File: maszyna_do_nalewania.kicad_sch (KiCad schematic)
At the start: 30 parts, among them J1 USB_C_Receptacle_USB2.0_16P, J2 SMA_RP, U1 ESP32-C3, Y1 40Mhz 10ppm

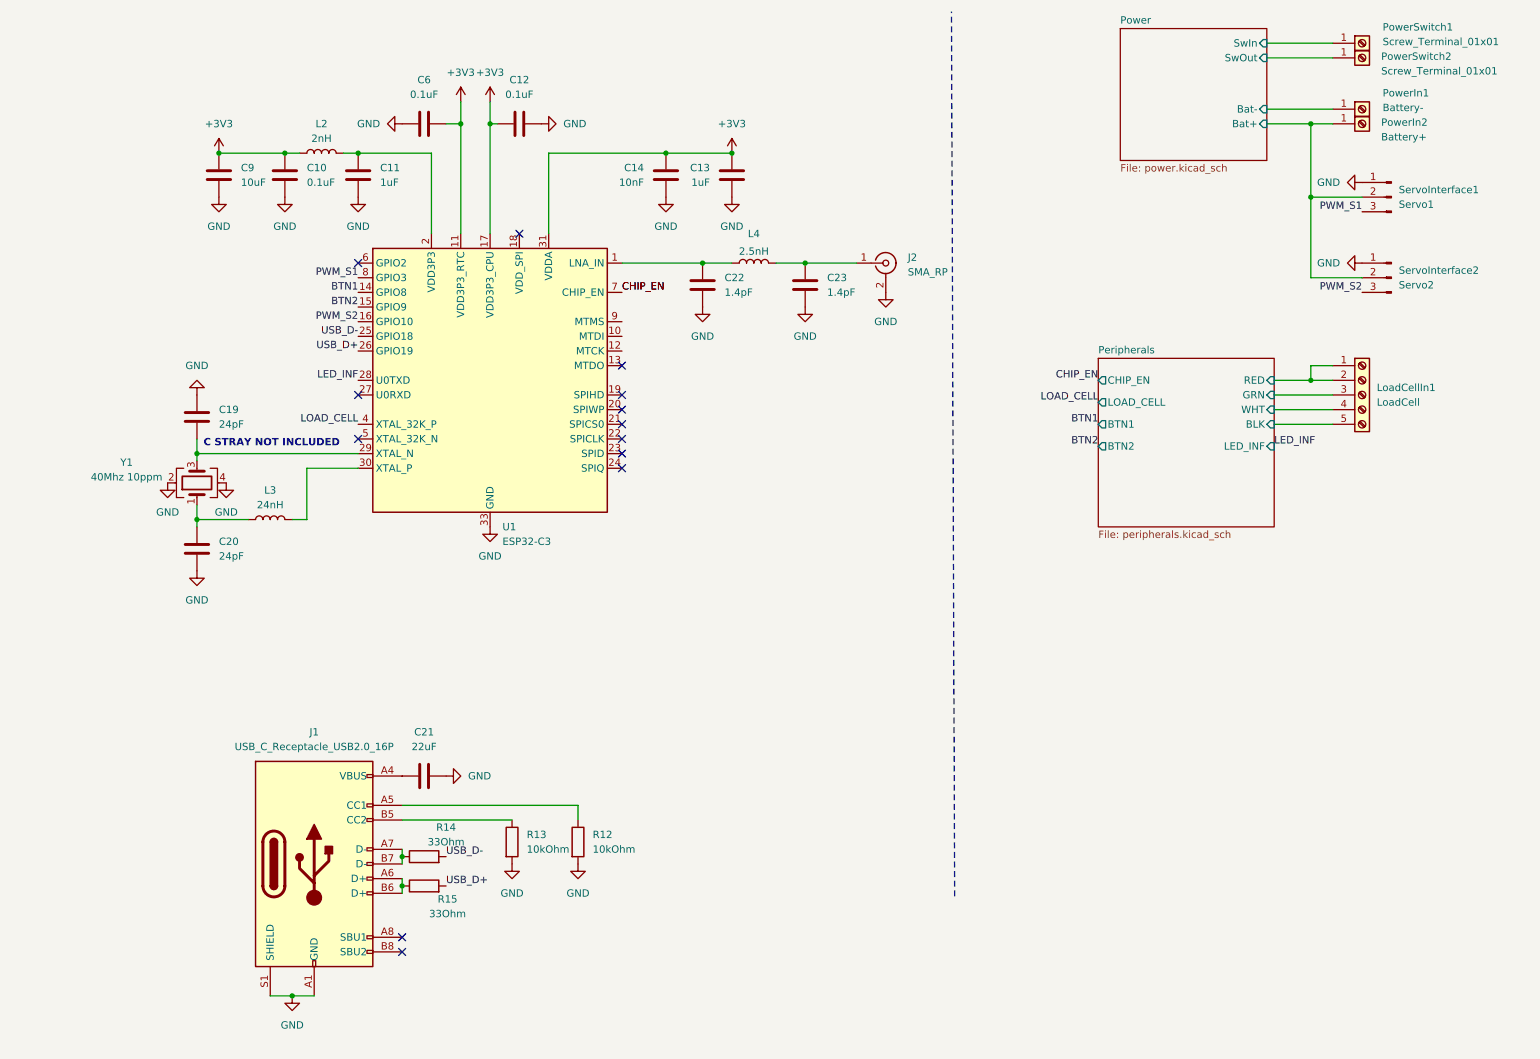
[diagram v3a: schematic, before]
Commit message: feat: pcb almost done, added rgb led
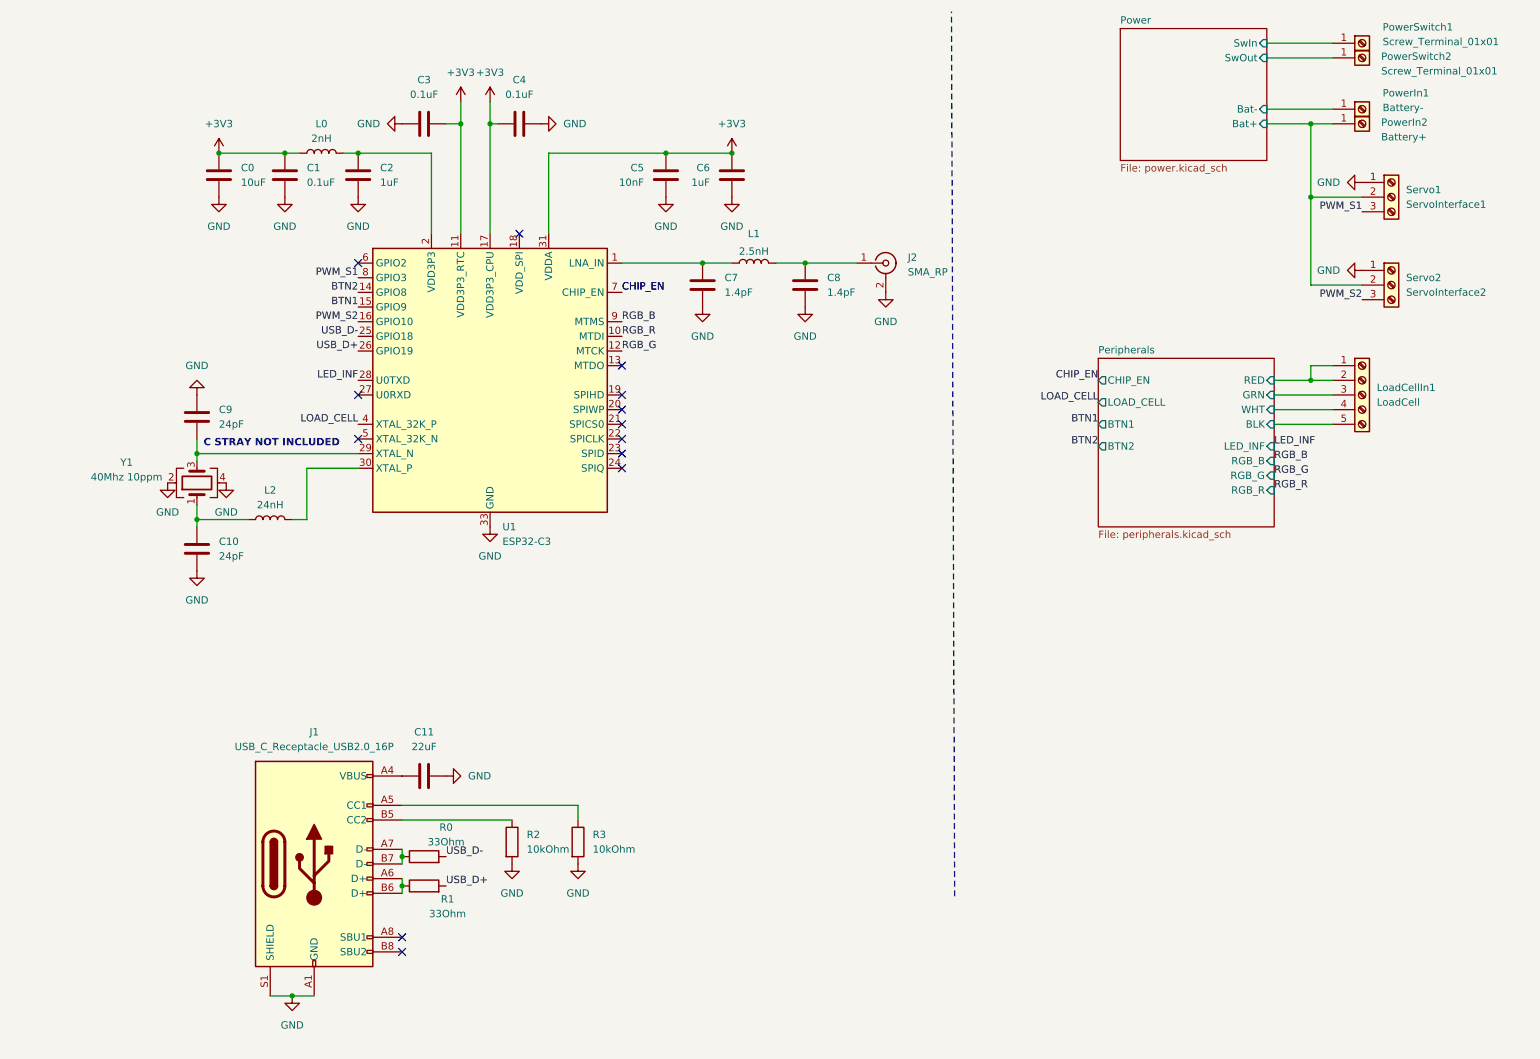
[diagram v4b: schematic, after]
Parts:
- removed ServoInterface1: Servo1, Connector_PinHeader_1.00mm:PinHeader_1x03_P1.00mm_Vertical, symbol Connector:Conn_01x03_Pin
- removed ServoInterface2: Servo2, Connector_PinHeader_1.00mm:PinHeader_1x03_P1.00mm_Vertical, symbol Connector:Conn_01x03_Pin
- added Servo1: ServoInterface1, TerminalBlock:TerminalBlock_MaiXu_MX126-5.0-03P_1x03_P5.00mm, symbol Connector:Screw_Terminal_01x03
- added Servo2: ServoInterface2, TerminalBlock:TerminalBlock_MaiXu_MX126-5.0-03P_1x03_P5.00mm, symbol Connector:Screw_Terminal_01x03
- C10: renamed from C20; footprint Capacitor_SMD:C_0805_2012Metric_Pad1.18x1.45mm_HandSolder -> Capacitor_SMD:C_0402_1005Metric
- C9: renamed from C19; footprint Capacitor_SMD:C_0805_2012Metric_Pad1.18x1.45mm_HandSolder -> Capacitor_SMD:C_0402_1005Metric
- R1: renamed from R15; footprint Resistor_SMD:R_0402_1005Metric_Pad0.72x0.64mm_HandSolder -> Resistor_SMD:R_0402_1005Metric
- renumbered C9 to C0, C10 to C1, C21 to C11, C11 to C2, C6 to C3, C12 to C4, C14 to C5, C13 to C6, C22 to C7, C23 to C8, L2 to L0, L4 to L1, L3 to L2, R14 to R0, R13 to R2, R12 to R3
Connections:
- net BTN1: now also U1.15 (GPIO9); no longer U1.14 (GPIO8)
- net BTN2: now also U1.14 (GPIO8); no longer U1.15 (GPIO9)
- net GND: now also Servo1.1 (Pin_1), Servo2.1 (Pin_1)
- net PWM_S1: now also Servo1.3 (Pin_3)
- net PWM_S2: now also Servo2.3 (Pin_3)
- net Power/Bat+: now also Servo1.2 (Pin_2), Servo2.2 (Pin_2)
- net RGB_R: now reaches U1.10 (MTDI)
- net RGB_G: now reaches U1.12 (MTCK)
- net RGB_B: now reaches U1.9 (MTMS)
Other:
- sheet Peripherals ports: added RGB_B, RGB_G, RGB_R; removed none

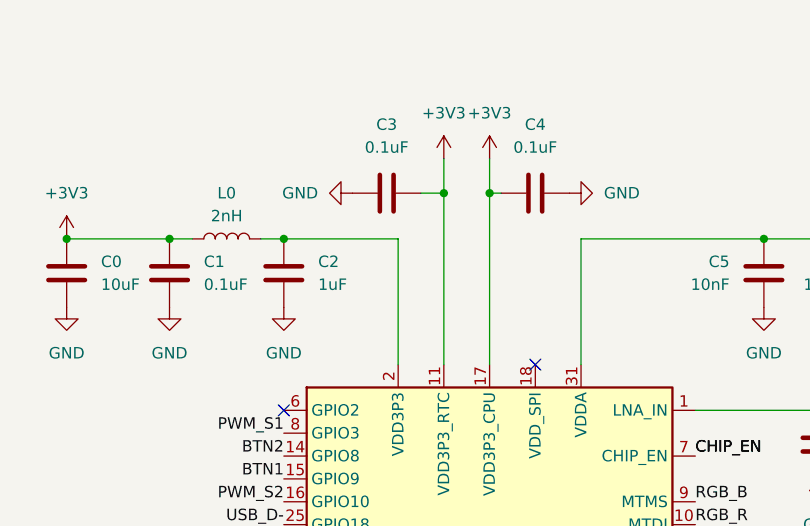
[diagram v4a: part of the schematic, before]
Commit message: feat: silkscreen done
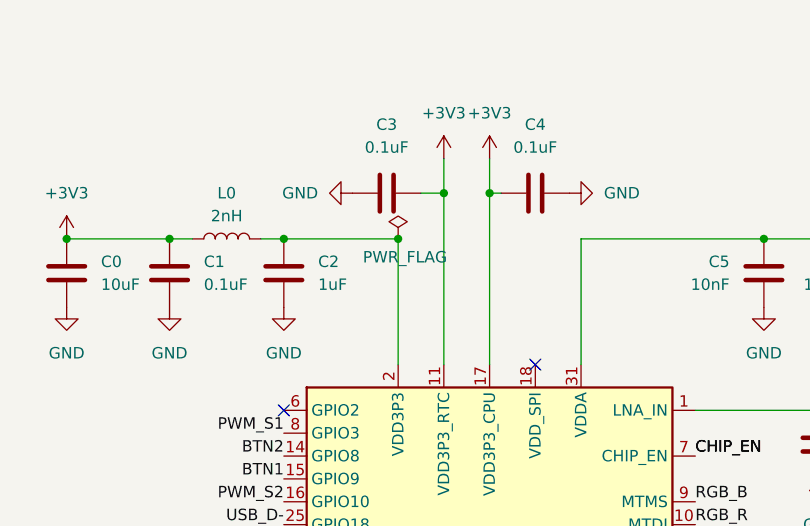
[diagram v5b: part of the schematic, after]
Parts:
- J1: footprint Connector_USB:USB_C_Receptacle_GCT_USB4085 -> Connector_USB:USB_C_Receptacle_HRO_TYPE-C-31-M-12
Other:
- company: (none) -> Mateusz Drogowski Karol Dworczyński
- title: (none) -> Drink Pouring Machine
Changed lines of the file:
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@@
 	(paper "A4")
 	(title_block
+		(title "Drink Pouring Machine")
 		(date "2025-12-08")
+		(rev "v1.0")
+		(company "Mateusz Drogowski Karol Dworczyński")
 	)
 	(text "C STRAY NOT INCLUDED"
@@
 		(color 0 0 0 0)
 	)
+	(junction
+		(at 86.36 36.83)
+		(diameter 0)
+		(color 0 0 0 0)
+	)
 	(no_connect
 		(at 73.66 86.36)
@@
 	)
 	(symbol
+		(lib_id "power:PWR_FLAG")
+		(at 86.36 36.83 0)
+		(unit 1)
+		(exclude_from_sim no)
+		(in_bom yes)
+		(on_board yes)
+		(dnp no)
+		(property "Reference" "#FLG04"
+			(at 86.36 34.925 0)
+			(effects
+				(font
+					(size 1.27 1.27)
+				)
+				(hide yes)
+			)
+		)
+		(property "Value" "PWR_FLAG"
+			(at 87.122 38.862 0)
+			(effects
+				(font
+					(size 1.27 1.27)
+				)
+			)
+		)
+		(property "Footprint" ""
+			(at 86.36 36.83 0)
+			(effects
+				(font
+					(size 1.27 1.27)
+				)
+				(hide yes)
+			)
+		)
+		(property "Datasheet" "~"
+			(at 86.36 36.83 0)
+			(effects
+				(font
+					(size 1.27 1.27)
+				)
+				(hide yes)
+			)
+		)
+		(property "Description" "Special symbol for telling ERC where power comes from"
+			(at 86.36 36.83 0)
+			(effects
+				(font
+					(size 1.27 1.27)
+				)
+				(hide yes)
+			)
+		)
+		(pin "1"
+		)
+		(instances
+			(project ""
+				(path "/9edf3a40-33ab-40a8-8c54-e53c70f0a44f"
+					(reference "#FLG04")
+					(unit 1)
+				)
+			)
+		)
+	)
+	(symbol
 		(lib_id "power:+3V3")
 		(at 138.43 36.83 0)
@@
 			)
 		)
-		(property "Footprint" "Connector_USB:USB_C_Receptacle_GCT_USB4085"
+		(property "Footprint" "Connector_USB:USB_C_Receptacle_HRO_TYPE-C-31-M-12"
 			(at 69.85 160.02 0)
 			(effects

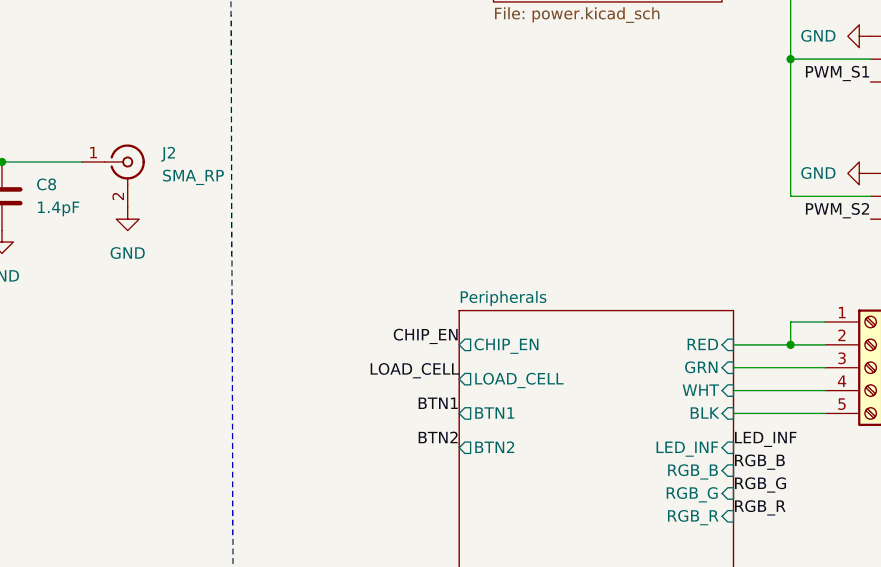
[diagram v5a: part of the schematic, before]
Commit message: fix: led resistor values, tensometer screw terminal
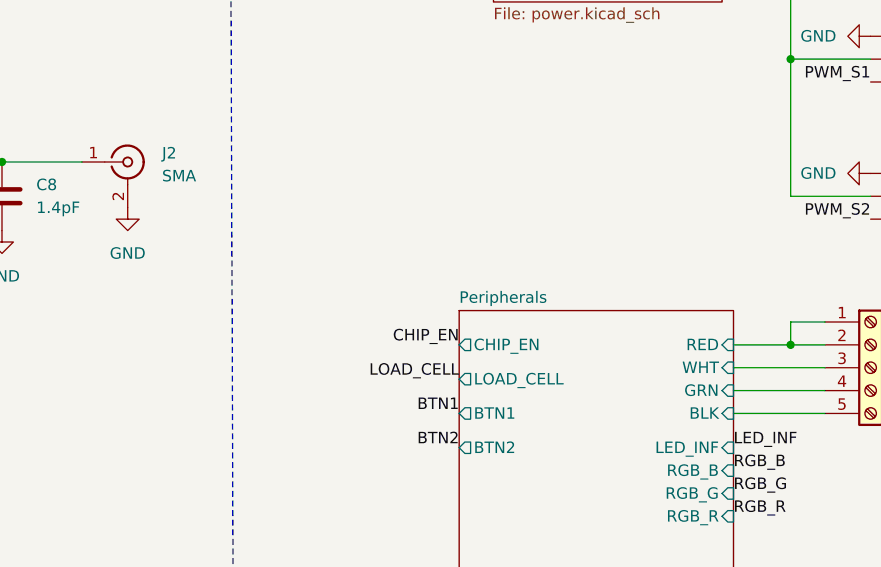
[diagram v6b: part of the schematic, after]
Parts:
- J2: value SMA_RP -> SMA
- LoadCellIn1: footprint TerminalBlock:TerminalBlock_MaiXu_MX126-5.0-05P_1x05_P5.00mm -> TerminalBlock_MetzConnect:TerminalBlock_MetzConnect_Type059_RT06305HBWC_1x05_P3.50mm_Horizontal
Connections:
- net Peripherals/GRN: now also LoadCellIn1.4 (Pin_4); no longer LoadCellIn1.3 (Pin_3)
- net Peripherals/WHT: now also LoadCellIn1.3 (Pin_3); no longer LoadCellIn1.4 (Pin_4)
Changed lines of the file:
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@@
 	(wire
 		(pts
+			(xy 232.41 81.28) (xy 242.57 81.28)
+		)
+		(stroke
+			(width 0)
+			(type default)
+		)
+	)
+	(wire
+		(pts
 			(xy 231.14 29.21) (xy 242.57 29.21)
 		)
@@
 	(wire
 		(pts
-			(xy 97.79 31.75) (xy 96.52 31.75)
+			(xy 232.41 78.74) (xy 242.57 78.74)
 		)
 		(stroke
@@
 	(wire
 		(pts
-			(xy 62.23 182.88) (xy 66.04 182.88)
+			(xy 97.79 31.75) (xy 96.52 31.75)
 		)
 		(stroke
@@
 	(wire
 		(pts
-			(xy 232.41 83.82) (xy 242.57 83.82)
+			(xy 62.23 182.88) (xy 66.04 182.88)
 		)
 		(stroke
@@
 	(wire
 		(pts
-			(xy 232.41 81.28) (xy 242.57 81.28)
+			(xy 232.41 83.82) (xy 242.57 83.82)
 		)
 		(stroke
@@
 	(wire
 		(pts
-			(xy 232.41 78.74) (xy 242.57 78.74)
-		)
-		(stroke
-			(width 0)
-			(type default)
-		)
-	)
-	(wire
-		(pts
 			(xy 231.14 20.32) (xy 242.57 20.32)
 		)
@@
 			)
 		)
-		(property "Footprint" "TerminalBlock:TerminalBlock_MaiXu_MX126-5.0-05P_1x05_P5.00mm"
+		(property "Footprint" "TerminalBlock_MetzConnect:TerminalBlock_MetzConnect_Type059_RT06305HBWC_1x05_P3.50mm_Horizontal"
 			(at 247.65 78.74 0)
 			(effects
@@
 			)
 		)
-		(property "Value" "SMA_RP"
+		(property "Value" "SMA"
 			(at 168.91 57.4431 0)
 			(effects
@@
 		)
 		(pin "GRN" input
-			(at 232.41 78.74 0)
+			(at 232.41 81.28 0)
 			(effects
 				(font
@@
 		)
 		(pin "WHT" input
-			(at 232.41 81.28 0)
+			(at 232.41 78.74 0)
 			(effects
 				(font
